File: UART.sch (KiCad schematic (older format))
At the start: 9 parts

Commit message: Erste fertige Version
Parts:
- removed R?: 10k, symbol Device:R_Small
- added D?: LED_Small, symbol Device:LED_Small
- added D?: D_Schottky_Small, symbol Device:D_Schottky_Small
- added R?: 47, symbol Device:R_Small
- added R?: 10k, symbol Device:R_Small
- added X?: XBee_S3, symbol HS-Wismar:XBee_S3
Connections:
- net +3V3: now also R?.1, X?.1 (VCC)
- net GND: now also R?.2, X?.10 (GND)
- net RX_in: now also X?.3 (DIN/~CONFIG~/DIO14)
- net TX_out: now also X?.2 (DOUT/DIO13)
- net ~RST: now also D?.1 (K)
- net at U?.1 (~RST): now also U?.4 (GPIO16), D?.2 (A), R?.2
- net at R?.2, SW?.2, U?.18 (GPIO0): now also X?.20 (AD0/DIO0)
- net at R?.2, SW?.2, U?.3 (EN): now also X?.5 (~RESET)
- net at U?.7 (GPIO13): now also D?.2 (A), X?.15 (ASSOCIATE/DIO5)
- new net: D?.1 (K), R?.1
- new net XBEE_RSSI: X?.6 (RSSI_PWM/DIO10)
- new net XBEE_Sleep_RQ: X?.9 (~DTR~/SLEEP_RQ/DIO8)
- new net XBEE_~CTS~: X?.12 (~CTS~/DIO7)
- new net XBEE_~RTS~: X?.16 (~RTS~/DIO6)
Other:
- moved on the sheet: C?, R?, SW?, U?

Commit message: Externe Spannungsversorgung
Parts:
- added C?: 100n, symbol Device:C_Small
- added J?: Conn_01x04_Male, symbol Connector:Conn_01x04_Male
- added J?: Conn_02x04_Odd_Even, symbol Connector_Generic:Conn_02x04_Odd_Even
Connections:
- net +3V3: now also C?.1, J?.3 (Pin_3)
- net GND: now also C?.2, J?.4 (Pin_4)
- net RX_in: now also J?.1 (Pin_1), J?.8 (Pin_8); no longer U?.21 (GPIO3/RXD), X?.3 (DIN/~CONFIG~/DIO14)
- net TX_out: now also J?.4 (Pin_4), J?.6 (Pin_6); no longer U?.22 (GPIO1/TXD), X?.2 (DOUT/DIO13)
- new net: J?.7 (Pin_7), U?.21 (GPIO3/RXD), X?.3 (DIN/~CONFIG~/DIO14)
- new net: J?.5 (Pin_5), U?.22 (GPIO1/TXD), X?.2 (DOUT/DIO13)
- new net: J?.1 (Pin_1), J?.2 (Pin_2)
- new net: J?.2 (Pin_2), J?.3 (Pin_3)
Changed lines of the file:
@@
 	0    -1   -1   0
 $EndComp
-Text HLabel 7800 2300 2    50   Input ~ 0
+Text HLabel 7800 2200 2    50   Input ~ 0
 RX_in
 Text HLabel 7800 2100 2    50   Output ~ 0
 TX_out
 Wire Wire Line
-	3850 2100 5650 2100
-Wire Wire Line
-	7800 2300 5750 2300
+	3850 2100 6500 2100
 $Comp
 L power:GND #PWR?
@@
 $EndComp
 Wire Wire Line
-	5650 2100 5650 4700
-Wire Wire Line
-	5650 4700 4650 4700
-Connection ~ 5650 2100
-Wire Wire Line
-	5650 2100 7800 2100
-Wire Wire Line
-	4650 4800 5750 4800
-Wire Wire Line
-	5750 4800 5750 2300
-Connection ~ 5750 2300
-Wire Wire Line
-	5750 2300 3850 2300
+	6500 2100 6500 4700
+Wire Wire Line
+	6500 4700 4650 4700
+Connection ~ 6500 2100
+Wire Wire Line
+	6500 2100 6950 2100
+Wire Wire Line
+	4650 4800 6600 4800
+Wire Wire Line
+	6600 4800 6600 2300
+Wire Wire Line
+	6600 2300 3850 2300
 $Comp
 L power:GND #PWR?
@@
 Wire Wire Line
 	2350 1850 2350 2000
+$Comp
+L Connector:Conn_01x04_Male J?
+U 1 1 5EFDB3FD
+P 5900 1650
+F 0 "J?" H 6008 1839 50  0000 C CNN
+F 1 "Conn_01x04_Male" H 6008 1840 50  0001 C CNN
+F 2 "" H 5900 1650 50  0001 C CNN
+F 3 "~" H 5900 1650 50  0001 C CNN
+	1    5900 1650
+	1    0    0    -1
+$EndComp
+$Comp
+L power:+3.3V #PWR?
+U 1 1 5EFE8401
+P 6200 1400
+F 0 "#PWR?" H 6200 1250 50  0001 C CNN
+F 1 "+3.3V" H 6215 1573 50  0000 C CNN
+F 2 "" H 6200 1400 50  0001 C CNN
+F 3 "" H 6200 1400 50  0001 C CNN
+	1    6200 1400
+	1    0    0    -1
+$EndComp
+Wire Wire Line
+	6200 1400 6200 1750
+Wire Wire Line
+	6200 1750 6100 1750
+$Comp
+L power:GND #PWR?
+U 1 1 5EFEB0C6
+P 6200 2400
+F 0 "#PWR?" H 6200 2150 50  0001 C CNN
+F 1 "GND" H 6205 2227 50  0000 C CNN
+F 2 "" H 6200 2400 50  0001 C CNN
+F 3 "" H 6200 2400 50  0001 C CNN
+	1    6200 2400
+	1    0    0    -1
+$EndComp
+Wire Wire Line
+	6200 2400 6200 1850
+Wire Wire Line
+	6200 1850 6100 1850
+$Comp
+L Device:C_Small C?
+U 1 1 5EFED216
+P 5650 1700
+F 0 "C?" V 5600 1550 50  0000 L CNN
+F 1 "100n" V 5600 1750 50  0000 L CNN
+F 2 "" H 5650 1700 50  0001 C CNN
+F 3 "~" H 5650 1700 50  0001 C CNN
+	1    5650 1700
+	1    0    0    -1
+$EndComp
+$Comp
+L power:+3.3V #PWR?
+U 1 1 5EFEE6C3
+P 5650 1400
+F 0 "#PWR?" H 5650 1250 50  0001 C CNN
+F 1 "+3.3V" H 5665 1573 50  0000 C CNN
+F 2 "" H 5650 1400 50  0001 C CNN
+F 3 "" H 5650 1400 50  0001 C CNN
+	1    5650 1400
+	1    0    0    -1
+$EndComp
+$Comp
+L power:GND #PWR?
+U 1 1 5EFF0343
+P 5650 2400
+F 0 "#PWR?" H 5650 2150 50  0001 C CNN
+F 1 "GND" H 5655 2227 50  0000 C CNN
+F 2 "" H 5650 2400 50  0001 C CNN
+F 3 "" H 5650 2400 50  0001 C CNN
+	1    5650 2400
+	1    0    0    -1
+$EndComp
+Wire Wire Line
+	5650 2400 5650 1800
+Wire Wire Line
+	5650 1600 5650 1400
+$Comp
+L Connector_Generic:Conn_02x04_Odd_Even J?
+U 1 1 5EFF7765
+P 7150 2000
+F 0 "J?" H 7200 2225 50  0000 C CNN
+F 1 "Conn_02x04_Odd_Even" H 7200 2226 50  0001 C CNN
+F 2 "" H 7150 2000 50  0001 C CNN
+F 3 "~" H 7150 2000 50  0001 C CNN
+	1    7150 2000
+	1    0    0    -1
+$EndComp
+Wire Wire Line
+	7450 2100 7600 2100
+Wire Wire Line
+	7800 2200 7600 2200
+Wire Wire Line
+	6950 2200 6600 2200
+Wire Wire Line
+	6600 2200 6600 2300
+Connection ~ 6600 2300
+Wire Wire Line
+	6950 2000 6700 2000
+Wire Wire Line
+	6700 2000 6700 1650
+Wire Wire Line
+	6700 1650 6100 1650
+Wire Wire Line
+	7450 1900 7600 1900
+Wire Wire Line
+	7600 1900 7600 1550
+Wire Wire Line
+	7600 1550 6100 1550
+Wire Wire Line
+	7450 2000 7600 2000
+Wire Wire Line
+	7600 2000 7600 2100
+Connection ~ 7600 2100
+Wire Wire Line
+	7600 2100 7800 2100
+Wire Wire Line
+	7600 2200 7600 2300
+Wire Wire Line
+	7600 2300 6850 2300
+Wire Wire Line
+	6850 2300 6850 1900
+Wire Wire Line
+	6850 1900 6950 1900
+Connection ~ 7600 2200
+Wire Wire Line
+	7600 2200 7450 2200
 $EndSCHEMATC

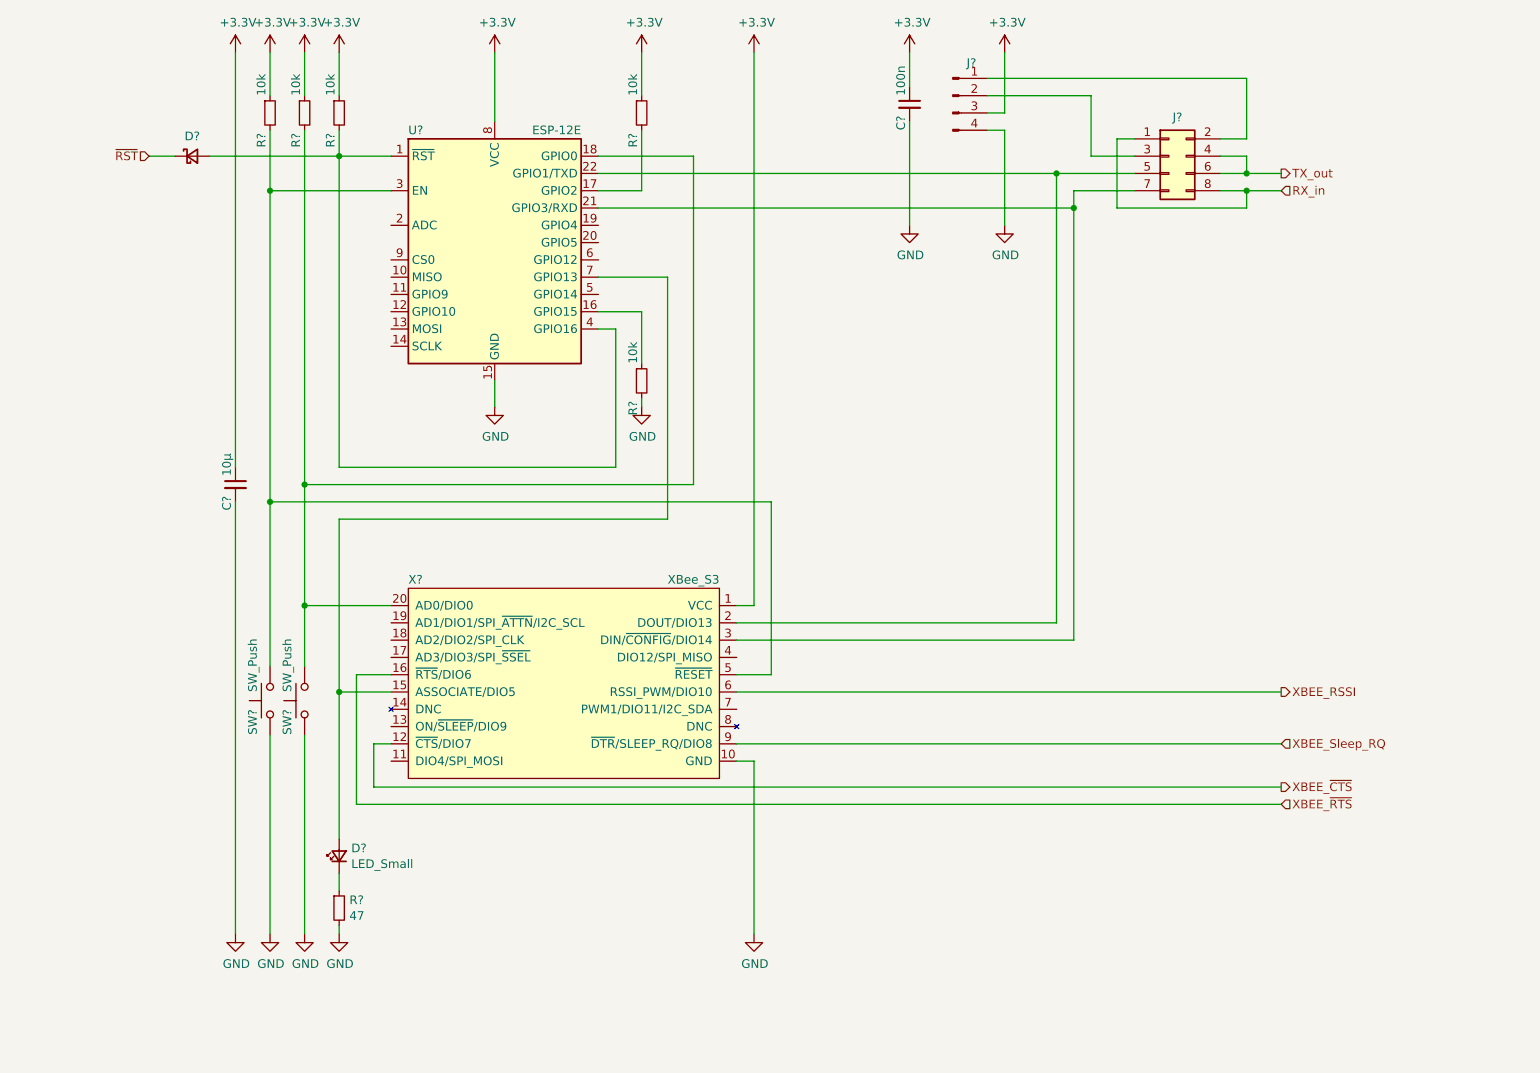
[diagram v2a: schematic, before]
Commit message: Bauteile grob platziert
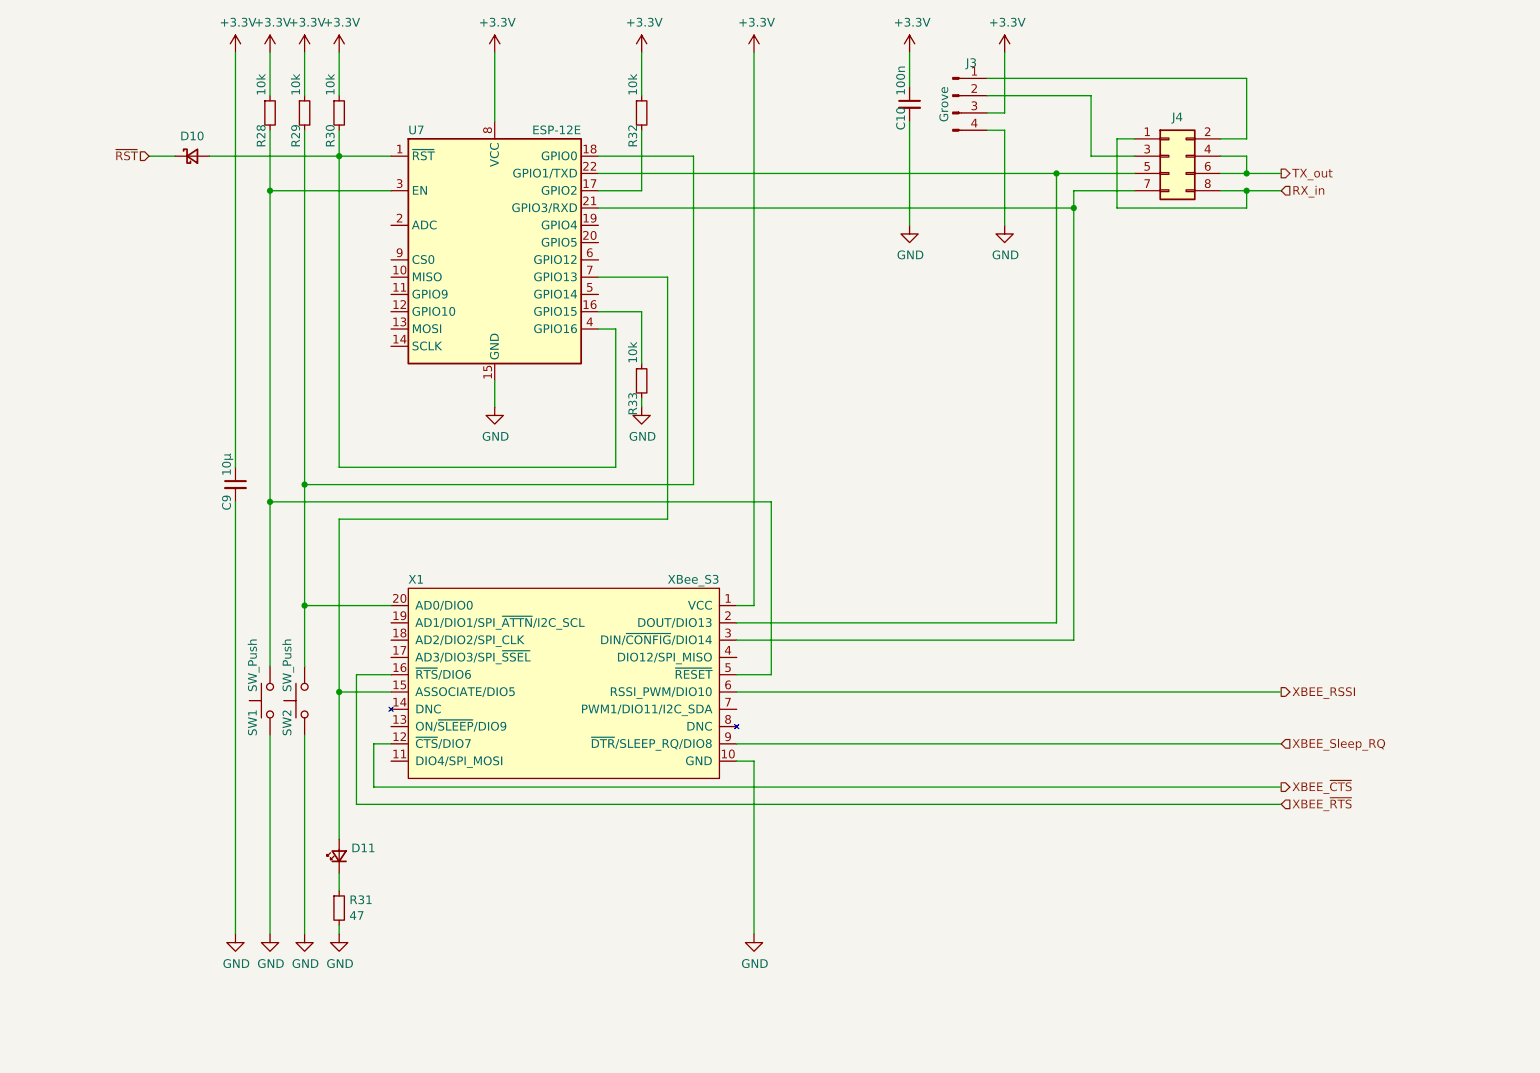
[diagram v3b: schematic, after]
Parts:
- C10: renamed from C?; footprint (none) -> Capacitor_SMD:C_0603_1608Metric_Pad1.05x0.95mm_HandSolder
- C9: renamed from C?; footprint (none) -> Capacitor_SMD:C_1206_3216Metric_Pad1.42x1.75mm_HandSolder
- D10: renamed from D?; footprint (none) -> Diode_SMD:D_SOD-123
- D11: renamed from D?; footprint (none) -> LED_SMD:LED_0603_1608Metric_Pad1.05x0.95mm_HandSolder
- J3: renamed from J?; value Conn_01x04_Male -> Grove; footprint (none) -> Connector:NS-Tech_Grove_1x04_P2mm_Vertical
- J4: renamed from J?; footprint (none) -> Connector_PinHeader_2.54mm:PinHeader_2x04_P2.54mm_Vertical
- R28, R29, R30, R31, R32, R33: renamed from R?; footprint (none) -> Resistor_SMD:R_0603_1608Metric_Pad1.05x0.95mm_HandSolder
- SW1, SW2: renamed from SW?; footprint (none) -> Button_Switch_THT:SW_Tactile_SPST_Angled_PTS645Vx39-2LFS
- X1: renamed from X?; footprint (none) -> HS-Wismar:XBEE_THT
- gave numbers to parts that had none: 1

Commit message: Alle Bauteile platziert
Alle Bauteile sind grob plaziert.
Einige Bauteile sollten noch umplaziert werden (u. a. die Jumper links neben Groov-Con, RGB-LED,).
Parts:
- C10, C9: symbol Device:C_Small -> MCT_Labor_5529-rescue:C_Small-Device
- D10: symbol Device:D_Schottky_Small -> MCT_Labor_5529-rescue:D_Schottky_Small-Device
- D11: symbol Device:LED_Small -> MCT_Labor_5529-rescue:LED_Small-Device
- J3: symbol Connector:Conn_01x04_Male -> MCT_Labor_5529-rescue:Conn_01x04_Male-Connector
- J4: symbol Connector_Generic:Conn_02x04_Odd_Even -> MCT_Labor_5529-rescue:Conn_02x04_Odd_Even-Connector_Generic
- R28, R29, R30, R31, R32, R33: symbol Device:R_Small -> MCT_Labor_5529-rescue:R_Small-Device
- SW1, SW2: symbol Switch:SW_Push -> MCT_Labor_5529-rescue:SW_Push-Switch
- U7: symbol RF_Module:ESP-12E -> MCT_Labor_5529-rescue:ESP-12E-RF_Module
- X1: symbol HS-Wismar:XBee_S3 -> MCT_Labor_5529-rescue:XBee_S3-HS-Wismar
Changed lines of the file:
@@
 $EndDescr
 $Comp
-L RF_Module:ESP-12E U7
+L MCT_Labor_5529-rescue:ESP-12E-RF_Module U7
 U 1 1 5EFB26CD
 P 3250 2600
@@
 $EndComp
 $Comp
-L power:+3.3V #PWR0147
+L MCT_Labor_5529-rescue:+3.3V-power #PWR0147
 U 1 1 5EFB3FB2
 P 3250 1400
@@
 	3250 1400 3250 1800
 $Comp
-L power:GND #PWR0148
+L MCT_Labor_5529-rescue:GND-power #PWR0148
 U 1 1 5EFB4472
 P 3250 3450
@@
 $EndComp
 $Comp
-L power:GND #PWR0149
+L MCT_Labor_5529-rescue:GND-power #PWR0149
 U 1 1 5EFB45D1
 P 1750 6500
@@
 	3250 3450 3250 3300
 $Comp
-L power:+3.3V #PWR0150
+L MCT_Labor_5529-rescue:+3.3V-power #PWR0150
 U 1 1 5EFB57D3
 P 1750 1400
@@
 $EndComp
 $Comp
-L Device:C_Small C9
+L MCT_Labor_5529-rescue:C_Small-Device C9
 U 1 1 5EFB5E54
 P 1750 3900
@@
 	1750 4000 1750 6500
 $Comp
-L Switch:SW_Push SW1
+L MCT_Labor_5529-rescue:SW_Push-Switch SW1
 U 1 1 5EFB889C
 P 1950 5150
@@
 	3850 2100 6500 2100
 $Comp
-L power:GND #PWR0151
+L MCT_Labor_5529-rescue:GND-power #PWR0151
 U 1 1 5EFBC55A
 P 1950 6500
@@
 $EndComp
 $Comp
-L Device:R_Small R28
+L MCT_Labor_5529-rescue:R_Small-Device R28
 U 1 1 5EFBC7DF
 P 1950 1750
@@
 $EndComp
 $Comp
-L power:+3.3V #PWR0152
+L MCT_Labor_5529-rescue:+3.3V-power #PWR0152
 U 1 1 5EFBD06D
 P 1950 1400
@@
 	1950 5350 1950 6500
 $Comp
-L Switch:SW_Push SW2
+L MCT_Labor_5529-rescue:SW_Push-Switch SW2
 U 1 1 5EFC6935
 P 2150 5150
@@
 $EndComp
 $Comp
-L power:GND #PWR0153
+L MCT_Labor_5529-rescue:GND-power #PWR0153
 U 1 1 5EFC693B
 P 2150 6500
@@
 	4400 2000 3850 2000
 $Comp
-L Device:R_Small R29
+L MCT_Labor_5529-rescue:R_Small-Device R29
 U 1 1 5EFC7DDD
 P 2150 1750
@@
 $EndComp
 $Comp
-L power:+3.3V #PWR0154
+L MCT_Labor_5529-rescue:+3.3V-power #PWR0154
 U 1 1 5EFC8779
 P 2150 1400
@@
 	2150 1400 2150 1650
 $Comp
-L Device:R_Small R32
+L MCT_Labor_5529-rescue:R_Small-Device R32
 U 1 1 5EFCB446
 P 4100 1750
@@
 $EndComp
 $Comp
-L power:+3.3V #PWR0155
+L MCT_Labor_5529-rescue:+3.3V-power #PWR0155
 U 1 1 5EFCB44D
 P 4100 1400
@@
 	4100 1850 4100 2200
 $Comp
-L Device:R_Small R33
+L MCT_Labor_5529-rescue:R_Small-Device R33
 U 1 1 5EFCE4CD
 P 4100 3300
@@
 $EndComp
 $Comp
-L power:GND #PWR0156
+L MCT_Labor_5529-rescue:GND-power #PWR0156
 U 1 1 5EFCE9EA
 P 4100 3450
@@
 	1250 2000 1400 2000
 $Comp
-L HS-Wismar:XBee_S3 X1
+L MCT_Labor_5529-rescue:XBee_S3-HS-Wismar X1
 U 1 1 5EFB500B
 P 4550 5600
@@
 	6600 2300 3850 2300
 $Comp
-L power:GND #PWR0157
+L MCT_Labor_5529-rescue:GND-power #PWR0157
 U 1 1 5EFC0DA6
 P 4750 6500
@@
 	4750 5500 4650 5500
 $Comp
-L power:+3.3V #PWR0158
+L MCT_Labor_5529-rescue:+3.3V-power #PWR0158
 U 1 1 5EFC1D3A
 P 4750 1400
@@
 	2450 5000 2650 5000
 $Comp
-L power:GND #PWR0159
+L MCT_Labor_5529-rescue:GND-power #PWR0159
 U 1 1 5EFC7534
 P 2350 6500
@@
 $EndComp
 $Comp
-L Device:R_Small R31
+L MCT_Labor_5529-rescue:R_Small-Device R31
 U 1 1 5EFC7A8E
 P 2350 6350
@@
 $EndComp
 $Comp
-L Device:LED_Small D11
+L MCT_Labor_5529-rescue:LED_Small-Device D11
 U 1 1 5EFC8488
 P 2350 6050
@@
 	2350 2000 2650 2000
 $Comp
-L Device:D_Schottky_Small D10
+L MCT_Labor_5529-rescue:D_Schottky_Small-Device D10
 U 1 1 5F596A7F
 P 1500 2000
@@
 Connection ~ 2350 5100
 $Comp
-L Device:R_Small R30
+L MCT_Labor_5529-rescue:R_Small-Device R30
 U 1 1 5F5A8C0A
 P 2350 1750
@@
 $EndComp
 $Comp
-L power:+3.3V #PWR0160
+L MCT_Labor_5529-rescue:+3.3V-power #PWR0160
 U 1 1 5F5A8C10
 P 2350 1400
@@
 	2350 1850 2350 2000
 $Comp
-L Connector:Conn_01x04_Male J3
+L MCT_Labor_5529-rescue:Conn_01x04_Male-Connector J3
 U 1 1 5EFDB3FD
 P 5900 1650
@@
 $EndComp
 $Comp
-L power:+3.3V #PWR0161
+L MCT_Labor_5529-rescue:+3.3V-power #PWR0161
 U 1 1 5EFE8401
 P 6200 1400
@@
 	6200 1750 6100 1750
 $Comp
-L power:GND #PWR0162
+L MCT_Labor_5529-rescue:GND-power #PWR0162
 U 1 1 5EFEB0C6
 P 6200 2400
@@
 	6200 1850 6100 1850
 $Comp
-L Device:C_Small C10
+L MCT_Labor_5529-rescue:C_Small-Device C10
 U 1 1 5EFED216
 P 5650 1700
@@
 $EndComp
 $Comp
-L power:+3.3V #PWR0163
+L MCT_Labor_5529-rescue:+3.3V-power #PWR0163
 U 1 1 5EFEE6C3
 P 5650 1400
@@
 $EndComp
 $Comp
-L power:GND #PWR0164
+L MCT_Labor_5529-rescue:GND-power #PWR0164
 U 1 1 5EFF0343
 P 5650 2400
@@
 	5650 1600 5650 1400
 $Comp
-L Connector_Generic:Conn_02x04_Odd_Even J4
+L MCT_Labor_5529-rescue:Conn_02x04_Odd_Even-Connector_Generic J4
 U 1 1 5EFF7765
 P 7150 2000

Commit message: minor glitches
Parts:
- removed D10: D_Schottky_Small, Diode_SMD:D_SOD-123, symbol MCT_Labor_5529-rescue:D_Schottky_Small-Device
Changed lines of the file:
@@
 Wire Wire Line
 	4100 2900 4100 3200
-Text HLabel 1250 2000 0    50   Input ~ 0
-~RST
-Wire Wire Line
-	1600 2000 2350 2000
-Wire Wire Line
-	1250 2000 1400 2000
 $Comp
 L MCT_Labor_5529-rescue:XBee_S3-HS-Wismar X1
@@
 Wire Wire Line
 	2350 2000 2650 2000
-$Comp
-L MCT_Labor_5529-rescue:D_Schottky_Small-Device D10
-U 1 1 5F596A7F
-P 1500 2000
-F 0 "D10" H 1500 2115 50  0000 C CNN
-F 1 "D_Schottky_Small" H 1500 2116 50  0001 C CNN
-F 2 "Diode_SMD:D_SOD-123" V 1500 2000 50  0001 C CNN
-F 3 "~" V 1500 2000 50  0001 C CNN
-	1    1500 2000
-	1    0    0    -1
-$EndComp
 Wire Wire Line
 	3850 2700 4250 2700
